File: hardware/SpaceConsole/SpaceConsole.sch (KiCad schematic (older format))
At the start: 0 parts

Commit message: Label all pins
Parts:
- added IC?: ArduinoProMini, mysensors_arduino:pro_mini_china, symbol mysensors_arduino:ArduinoProMini
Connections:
- new net GND: IC?.24 (RAW)
- new net HornOut: IC?.17 ((PCINT8/ADC0)PC0/14/A0)
- new net KnobA0: IC?.13 ((PCINT2/OC1B/~SS~/PWM)PB2/10)
- new net KnobA1: IC?.14 ((PCINT3/OC2A/MOSI/PWM)PB3/11)
- new net KnobB0: IC?.15 ((PCINT4/MISO)PB4/12)
- new net KnobB1: IC?.16 ((PCINT5/SCK)PB5/13)
- new net LeftFrontLED: IC?.5 ((PCINT18/INT0)PD2/2)
- new net LeftMiddleLED: IC?.7 ((PCINT20/XCK/T0)PD4/4)
- new net RearLED: IC?.9 ((PCINT22/OC0A/AIN0/PWM)PD6/6)
- new net RightFrontLED: IC?.6 ((PCINT19/OC2B/INT1/PWM)PD3/3)
- new net RightMiddleLED: IC?.8 ((PCINT21/OC0B/T1/PWM)PD5/5)
- new net SwitchA: IC?.10 ((PCINT23/AIN1)PD7/7)
- new net SwitchB: IC?.11 ((PCINT0/CLKO/ICP1)PB0/8)
- new net SwitchC: IC?.12 ((PCINT1/OC1A/PWM)PB1/9)
- new net VCC: IC?.21 (VCC)
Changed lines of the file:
@@
 Comment4 ""
 $EndDescr
+$Comp
+L mysensors_arduino:ArduinoProMini IC?
+U 1 1 5FB7EAFA
+P 5250 4150
+F 0 "IC?" H 5300 5600 40  0000 C CNN
+F 1 "ArduinoProMini" H 5300 5524 40  0000 C CNN
+F 2 "mysensors_arduino:pro_mini_china" H 5250 4150 30  0001 C CIN
+F 3 "http://www.arduino.cc/en/uploads/Main/Arduino-Pro-Mini-schematic.pdf" H 5300 5433 60  0000 C CNN
+	1    5250 4150
+	1    0    0    -1
+$EndComp
+$Comp
+L power:VCC #PWR?
+U 1 1 5FB7FD72
+P 4350 3050
+F 0 "#PWR?" H 4350 2900 50  0001 C CNN
+F 1 "VCC" V 4365 3177 50  0000 L CNN
+F 2 "" H 4350 3050 50  0001 C CNN
+F 3 "" H 4350 3050 50  0001 C CNN
+	1    4350 3050
+	0    -1   -1   0
+$EndComp
+$Comp
+L power:GND #PWR?
+U 1 1 5FB80DDB
+P 4350 3350
+F 0 "#PWR?" H 4350 3100 50  0001 C CNN
+F 1 "GND" V 4355 3222 50  0000 R CNN
+F 2 "" H 4350 3350 50  0001 C CNN
+F 3 "" H 4350 3350 50  0001 C CNN
+	1    4350 3350
+	0    1    1    0
+$EndComp
+Text Label 6250 3250 0    50   ~ 0
+LeftFrontLED
+Text Label 6250 3350 0    50   ~ 0
+RightFrontLED
+Text Label 6250 3450 0    50   ~ 0
+LeftMiddleLED
+Text Label 6250 3550 0    50   ~ 0
+RightMiddleLED
+Text Label 6250 3650 0    50   ~ 0
+RearLED
+Text Label 6250 3750 0    50   ~ 0
+SwitchA
+Text Label 6250 3850 0    50   ~ 0
+SwitchB
+Text Label 6250 3950 0    50   ~ 0
+SwitchC
+Text Label 6250 4650 0    50   ~ 0
+HornOut
+Text Label 6250 4450 0    50   ~ 0
+KnobB1
+Text Label 6250 4350 0    50   ~ 0
+KnobB0
+Text Label 6250 4250 0    50   ~ 0
+KnobA1
+Text Label 6250 4050 0    50   ~ 0
+KnobA0
 $EndSCHEMATC

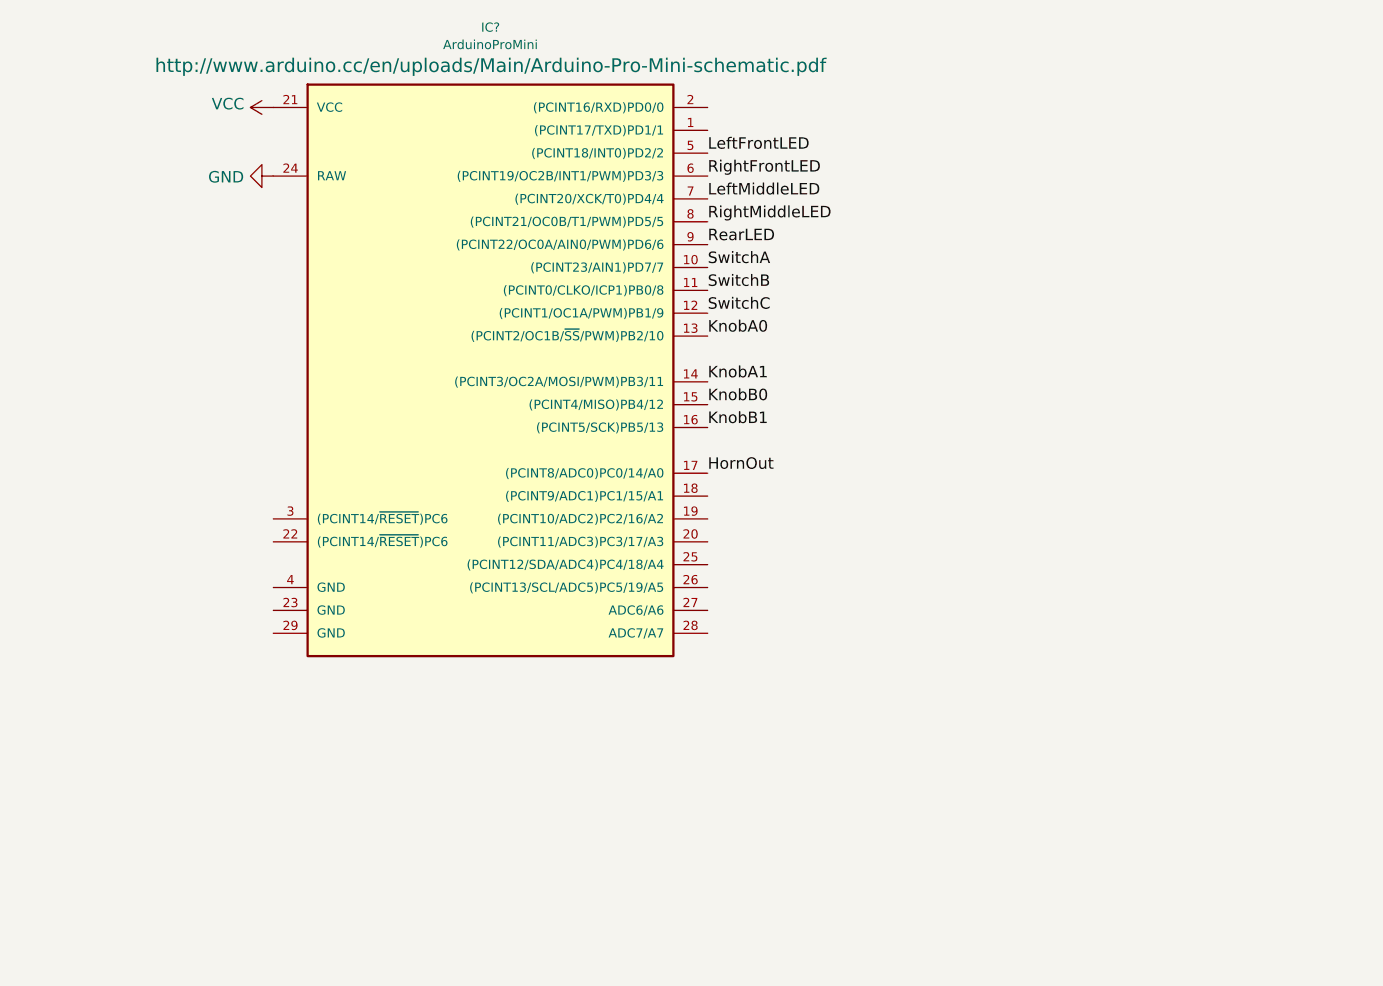
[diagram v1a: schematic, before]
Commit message: Add screw terminals
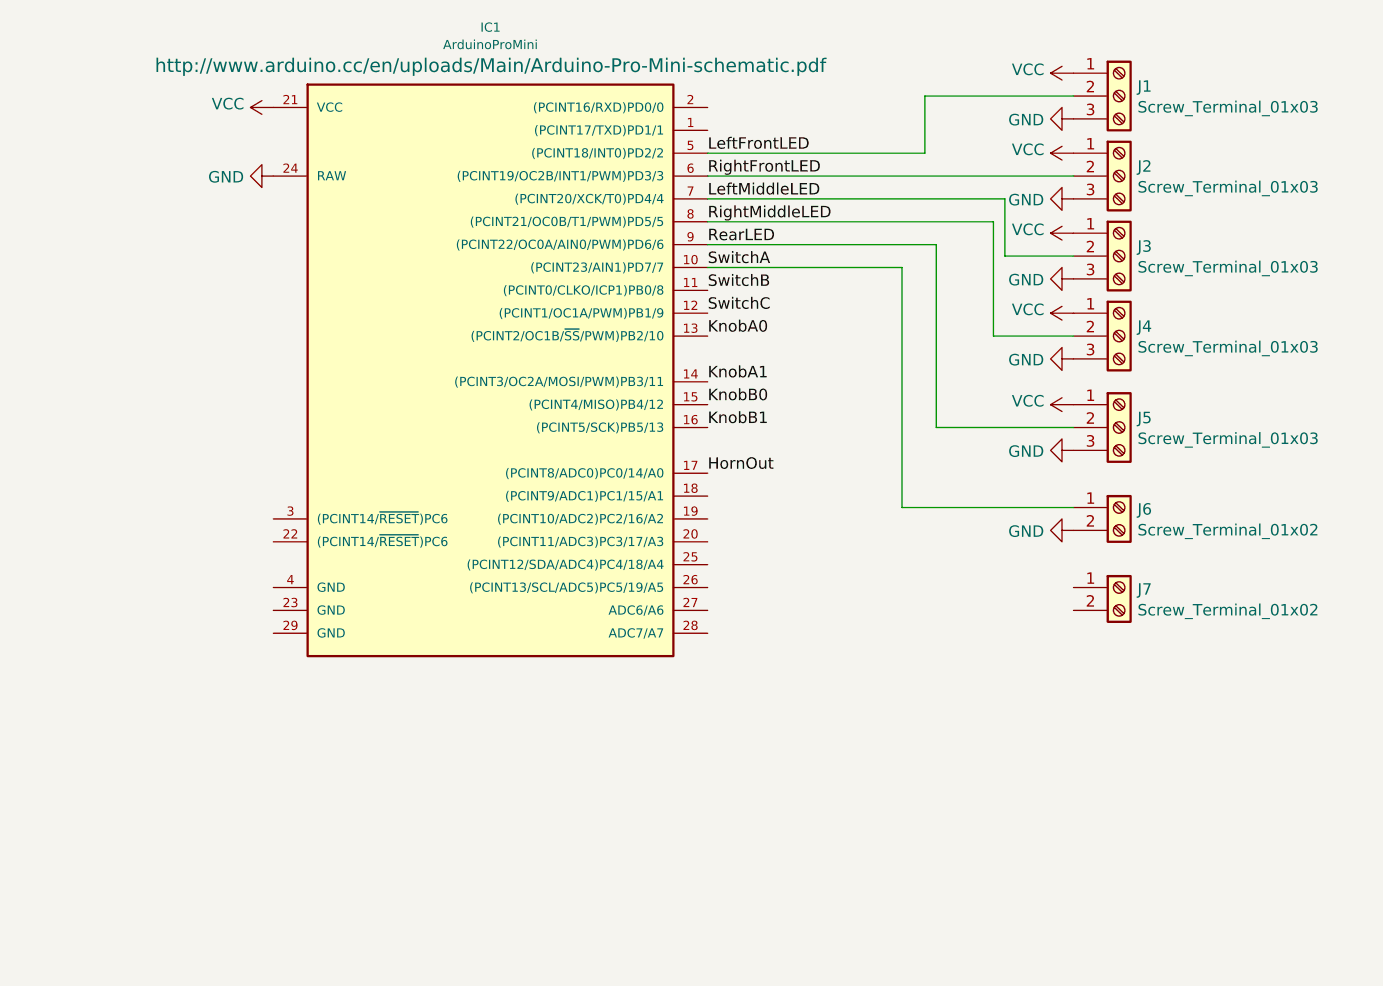
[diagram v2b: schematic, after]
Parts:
- added J1, J2, J3, J4, J5: Screw_Terminal_01x03, symbol Connector:Screw_Terminal_01x03
- added J6, J7: Screw_Terminal_01x02, symbol Connector:Screw_Terminal_01x02
- gave numbers to parts that had none: 1
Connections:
- net GND: now also J1.3 (Pin_3), J2.3 (Pin_3), J3.3 (Pin_3), J4.3 (Pin_3), J5.3 (Pin_3), J6.2 (Pin_2)
- net LeftFrontLED: now also J1.2 (Pin_2)
- net LeftMiddleLED: now also J3.2 (Pin_2)
- net RearLED: now also J5.2 (Pin_2)
- net RightFrontLED: now also J2.2 (Pin_2)
- net RightMiddleLED: now also J4.2 (Pin_2)
- net SwitchA: now also J6.1 (Pin_1)
- net VCC: now also J1.1 (Pin_1), J2.1 (Pin_1), J3.1 (Pin_1), J4.1 (Pin_1), J5.1 (Pin_1)
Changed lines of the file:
@@
 $EndDescr
 $Comp
-L mysensors_arduino:ArduinoProMini IC?
+L mysensors_arduino:ArduinoProMini IC1
 U 1 1 5FB7EAFA
 P 5250 4150
-F 0 "IC?" H 5300 5600 40  0000 C CNN
+F 0 "IC1" H 5300 5600 40  0000 C CNN
 F 1 "ArduinoProMini" H 5300 5524 40  0000 C CNN
 F 2 "mysensors_arduino:pro_mini_china" H 5250 4150 30  0001 C CIN
@@
 $EndComp
 $Comp
-L power:VCC #PWR?
+L power:VCC #PWR01
 U 1 1 5FB7FD72
 P 4350 3050
-F 0 "#PWR?" H 4350 2900 50  0001 C CNN
+F 0 "#PWR01" H 4350 2900 50  0001 C CNN
 F 1 "VCC" V 4365 3177 50  0000 L CNN
 F 2 "" H 4350 3050 50  0001 C CNN
@@
 $EndComp
 $Comp
-L power:GND #PWR?
+L power:GND #PWR02
 U 1 1 5FB80DDB
 P 4350 3350
-F 0 "#PWR?" H 4350 3100 50  0001 C CNN
+F 0 "#PWR02" H 4350 3100 50  0001 C CNN
 F 1 "GND" V 4355 3222 50  0000 R CNN
 F 2 "" H 4350 3350 50  0001 C CNN
@@
 Text Label 6250 4050 0    50   ~ 0
 KnobA0
+$Comp
+L Connector:Screw_Terminal_01x03 J1
+U 1 1 5FB82450
+P 8050 3000
+F 0 "J1" H 8130 3042 50  0000 L CNN
+F 1 "Screw_Terminal_01x03" H 8130 2951 50  0000 L CNN
+F 2 "" H 8050 3000 50  0001 C CNN
+F 3 "~" H 8050 3000 50  0001 C CNN
+	1    8050 3000
+	1    0    0    -1
+$EndComp
+$Comp
+L Connector:Screw_Terminal_01x03 J2
+U 1 1 5FB83151
+P 8050 3350
+F 0 "J2" H 8130 3392 50  0000 L CNN
+F 1 "Screw_Terminal_01x03" H 8130 3301 50  0000 L CNN
+F 2 "" H 8050 3350 50  0001 C CNN
+F 3 "~" H 8050 3350 50  0001 C CNN
+	1    8050 3350
+	1    0    0    -1
+$EndComp
+$Comp
+L Connector:Screw_Terminal_01x03 J3
+U 1 1 5FB83CFA
+P 8050 3700
+F 0 "J3" H 8130 3742 50  0000 L CNN
+F 1 "Screw_Terminal_01x03" H 8130 3651 50  0000 L CNN
+F 2 "" H 8050 3700 50  0001 C CNN
+F 3 "~" H 8050 3700 50  0001 C CNN
+	1    8050 3700
+	1    0    0    -1
+$EndComp
+$Comp
+L Connector:Screw_Terminal_01x03 J4
+U 1 1 5FB847FB
+P 8050 4050
+F 0 "J4" H 8130 4092 50  0000 L CNN
+F 1 "Screw_Terminal_01x03" H 8130 4001 50  0000 L CNN
+F 2 "" H 8050 4050 50  0001 C CNN
+F 3 "~" H 8050 4050 50  0001 C CNN
+	1    8050 4050
+	1    0    0    -1
+$EndComp
+$Comp
+L Connector:Screw_Terminal_01x03 J5
+U 1 1 5FB8539C
+P 8050 4450
+F 0 "J5" H 8130 4492 50  0000 L CNN
+F 1 "Screw_Terminal_01x03" H 8130 4401 50  0000 L CNN
+F 2 "" H 8050 4450 50  0001 C CNN
+F 3 "~" H 8050 4450 50  0001 C CNN
+	1    8050 4450
+	1    0    0    -1
+$EndComp
+Wire Wire Line
+	6250 3250 7200 3250
+Wire Wire Line
+	6250 3350 7850 3350
+Wire Wire Line
+	6250 3550 7500 3550
+Wire Wire Line
+	6250 3650 7250 3650
+Wire Wire Line
+	7250 3650 7250 4450
+Wire Wire Line
+	7500 3550 7500 4050
+Wire Wire Line
+	7500 4050 7850 4050
+Wire Wire Line
+	7250 4450 7850 4450
+Wire Wire Line
+	7200 3250 7200 3000
+Wire Wire Line
+	7200 3000 7850 3000
+$Comp
+L Connector:Screw_Terminal_01x02 J6
+U 1 1 5FB9702F
+P 8050 4800
+F 0 "J6" H 8130 4792 50  0000 L CNN
+F 1 "Screw_Terminal_01x02" H 8130 4701 50  0000 L CNN
+F 2 "" H 8050 4800 50  0001 C CNN
+F 3 "~" H 8050 4800 50  0001 C CNN
+	1    8050 4800
+	1    0    0    -1
+$EndComp
+$Comp
+L Connector:Screw_Terminal_01x02 J7
+U 1 1 5FB97F65
+P 8050 5150
+F 0 "J7" H 8130 5142 50  0000 L CNN
+F 1 "Screw_Terminal_01x02" H 8130 5051 50  0000 L CNN
+F 2 "" H 8050 5150 50  0001 C CNN
+F 3 "~" H 8050 5150 50  0001 C CNN
+	1    8050 5150
+	1    0    0    -1
+$EndComp
+Wire Wire Line
+	6250 3750 7100 3750
+Wire Wire Line
+	7100 3750 7100 4800
+Wire Wire Line
+	7100 4800 7850 4800
+$Comp
+L power:GND #PWR03
+U 1 1 5FB99262
+P 7850 4900
+F 0 "#PWR03" H 7850 4650 50  0001 C CNN
+F 1 "GND" V 7855 4772 50  0000 R CNN
+F 2 "" H 7850 4900 50  0001 C CNN
+F 3 "" H 7850 4900 50  0001 C CNN
+	1    7850 4900
+	0    1    1    0
+$EndComp
+$Comp
+L power:GND #PWR?
+U 1 1 5FB9B39A
+P 7850 3100
+F 0 "#PWR?" H 7850 2850 50  0001 C CNN
+F 1 "GND" V 7855 2972 50  0000 R CNN
+F 2 "" H 7850 3100 50  0001 C CNN
+F 3 "" H 7850 3100 50  0001 C CNN
+	1    7850 3100
+	0    1    1    0
+$EndComp
+$Comp
+L power:GND #PWR?
+U 1 1 5FB9BFBF
+P 7850 3450
+F 0 "#PWR?" H 7850 3200 50  0001 C CNN
+F 1 "GND" V 7855 3322 50  0000 R CNN
+F 2 "" H 7850 3450 50  0001 C CNN
+F 3 "" H 7850 3450 50  0001 C CNN
+	1    7850 3450
+	0    1    1    0
+$EndComp
+$Comp
+L power:GND #PWR?
+U 1 1 5FB9C2F9
+P 7850 3800
+F 0 "#PWR?" H 7850 3550 50  0001 C CNN
+F 1 "GND" V 7855 3672 50  0000 R CNN
+F 2 "" H 7850 3800 50  0001 C CNN
+F 3 "" H 7850 3800 50  0001 C CNN
+	1    7850 3800
+	0    1    1    0
+$EndComp
+$Comp
+L power:GND #PWR?
+U 1 1 5FB9C647
+P 7850 4150
+F 0 "#PWR?" H 7850 3900 50  0001 C CNN
+F 1 "GND" V 7855 4022 50  0000 R CNN
+F 2 "" H 7850 4150 50  0001 C CNN
+F 3 "" H 7850 4150 50  0001 C CNN
+	1    7850 4150
+	0    1    1    0
+$EndComp
+$Comp
+L power:GND #PWR?
+U 1 1 5FB9CF71
+P 7850 4550
+F 0 "#PWR?" H 7850 4300 50  0001 C CNN
+F 1 "GND" V 7855 4422 50  0000 R CNN
+F 2 "" H 7850 4550 50  0001 C CNN
+F 3 "" H 7850 4550 50  0001 C CNN
+	1    7850 4550
+	0    1    1    0
+$EndComp
+$Comp
+L power:VCC #PWR?
+U 1 1 5FB9D84A
+P 7850 2900
+F 0 "#PWR?" H 7850 2750 50  0001 C CNN
+F 1 "VCC" V 7865 3027 50  0000 L CNN
+F 2 "" H 7850 2900 50  0001 C CNN
+F 3 "" H 7850 2900 50  0001 C CNN
+	1    7850 2900
+	0    -1   -1   0
+$EndComp
+$Comp
+L power:VCC #PWR?
+U 1 1 5FB9E272
+P 7850 3250
+F 0 "#PWR?" H 7850 3100 50  0001 C CNN
+F 1 "VCC" V 7865 3377 50  0000 L CNN
+F 2 "" H 7850 3250 50  0001 C CNN
+F 3 "" H 7850 3250 50  0001 C CNN
+	1    7850 3250
+	0    -1   -1   0
+$EndComp
+$Comp
+L power:VCC #PWR?
+U 1 1 5FB9EB8F
+P 7850 3600
+F 0 "#PWR?" H 7850 3450 50  0001 C CNN
+F 1 "VCC" V 7865 3727 50  0000 L CNN
+F 2 "" H 7850 3600 50  0001 C CNN
+F 3 "" H 7850 3600 50  0001 C CNN
+	1    7850 3600
+	0    -1   -1   0
+$EndComp
+$Comp
+L power:VCC #PWR?
+U 1 1 5FB9F00F
+P 7850 3950
+F 0 "#PWR?" H 7850 3800 50  0001 C CNN
+F 1 "VCC" V 7865 4077 50  0000 L CNN
+F 2 "" H 7850 3950 50  0001 C CNN
+F 3 "" H 7850 3950 50  0001 C CNN
+	1    7850 3950
+	0    -1   -1   0
+$EndComp
+$Comp
+L power:VCC #PWR?
+U 1 1 5FB9F5DF
+P 7850 4350
+F 0 "#PWR?" H 7850 4200 50  0001 C CNN
+F 1 "VCC" V 7865 4477 50  0000 L CNN
+F 2 "" H 7850 4350 50  0001 C CNN
+F 3 "" H 7850 4350 50  0001 C CNN
+	1    7850 4350
+	0    -1   -1   0
+$EndComp
+Wire Wire Line
+	7550 3700 7850 3700
+Wire Wire Line
+	6250 3450 7550 3450
+Wire Wire Line
+	7550 3450 7550 3700
 $EndSCHEMATC

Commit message: Add switching regulator and lib
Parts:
- added U?: LM2596_Adj_Stepdown_Module, symbol myComponents:LM2596_Adj_Stepdown_Module
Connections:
- net GND: now also U?.4 (OUT-)
- net VCC: now also U?.3 (OUT+)
- net Battery+: now reaches J7.1 (Pin_1)
- net Battery+: now also U?.1 (IN+)
- net Battery-: now reaches J7.2 (Pin_2)
- net Battery-: now also U?.2 (IN-)
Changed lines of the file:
@@
 Wire Wire Line
 	7550 3450 7550 3700
+$Comp
+L myComponents:LM2596_Adj_Stepdown_Module U?
+U 1 1 5FBA7ED4
+P 7200 5650
+F 0 "U?" H 7428 5326 50  0000 L CNN
+F 1 "LM2596_Adj_Stepdown_Module" H 7428 5235 50  0000 L CNN
+F 2 "" H 7200 5650 50  0001 C CNN
+F 3 "" H 7200 5650 50  0001 C CNN
+	1    7200 5650
+	1    0    0    -1
+$EndComp
+$Comp
+L power:VCC #PWR?
+U 1 1 5FBA8E0E
+P 6950 6100
+F 0 "#PWR?" H 6950 5950 50  0001 C CNN
+F 1 "VCC" V 6965 6227 50  0000 L CNN
+F 2 "" H 6950 6100 50  0001 C CNN
+F 3 "" H 6950 6100 50  0001 C CNN
+	1    6950 6100
+	0    -1   -1   0
+$EndComp
+$Comp
+L power:GND #PWR?
+U 1 1 5FBAA224
+P 6950 6250
+F 0 "#PWR?" H 6950 6000 50  0001 C CNN
+F 1 "GND" V 6955 6122 50  0000 R CNN
+F 2 "" H 6950 6250 50  0001 C CNN
+F 3 "" H 6950 6250 50  0001 C CNN
+	1    6950 6250
+	0    1    1    0
+$EndComp
+Text Label 7850 5150 2    50   ~ 0
+Battery+
+Text Label 6950 5800 2    50   ~ 0
+Battery+
+Text Label 7850 5250 2    50   ~ 0
+Battery-
+Text Label 6950 5950 2    50   ~ 0
+Battery-
 $EndSCHEMATC

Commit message: Add Know/switch headers
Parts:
- added J?: Conn_01x09_Male, symbol Connector:Conn_01x09_Male
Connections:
- net GND: now also J?.1 (Pin_1)
- net HornOut: now also J?.9 (Pin_9)
- net KnobA0: now also J?.5 (Pin_5)
- net KnobA1: now also J?.6 (Pin_6)
- net KnobB0: now also J?.7 (Pin_7)
- net KnobB1: now also J?.8 (Pin_8)
- net SwitchB: now also J?.3 (Pin_3)
- net SwitchC: now also J?.4 (Pin_4)
- net VCC: now also J?.2 (Pin_2)
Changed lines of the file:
@@
 Text Label 6950 5950 2    50   ~ 0
 Battery-
+$Comp
+L Connector:Conn_01x09_Male J?
+U 1 1 5FBB2A1F
+P 5450 6400
+F 0 "J?" H 5558 6981 50  0000 C CNN
+F 1 "Conn_01x09_Male" H 5558 6890 50  0000 C CNN
+F 2 "" H 5450 6400 50  0001 C CNN
+F 3 "~" H 5450 6400 50  0001 C CNN
+	1    5450 6400
+	1    0    0    -1
+$EndComp
+$Comp
+L power:GND #PWR?
+U 1 1 5FBB4227
+P 5650 6000
+F 0 "#PWR?" H 5650 5750 50  0001 C CNN
+F 1 "GND" V 5655 5872 50  0000 R CNN
+F 2 "" H 5650 6000 50  0001 C CNN
+F 3 "" H 5650 6000 50  0001 C CNN
+	1    5650 6000
+	0    -1   -1   0
+$EndComp
+$Comp
+L power:VCC #PWR?
+U 1 1 5FBB4E89
+P 5650 6100
+F 0 "#PWR?" H 5650 5950 50  0001 C CNN
+F 1 "VCC" V 5665 6228 50  0000 L CNN
+F 2 "" H 5650 6100 50  0001 C CNN
+F 3 "" H 5650 6100 50  0001 C CNN
+	1    5650 6100
+	0    1    1    0
+$EndComp
+Text Label 5650 6200 0    50   ~ 0
+SwitchB
+Text Label 5650 6300 0    50   ~ 0
+SwitchC
+Text Label 5650 6400 0    50   ~ 0
+KnobA0
+Text Label 5650 6500 0    50   ~ 0
+KnobA1
+Text Label 5650 6600 0    50   ~ 0
+KnobB0
+Text Label 5650 6700 0    50   ~ 0
+KnobB1
+Text Label 5650 6800 0    50   ~ 0
+HornOut
 $EndSCHEMATC
